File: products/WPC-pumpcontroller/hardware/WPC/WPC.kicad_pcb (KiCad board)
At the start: 2 copper layers, 97.4 x 49.1 mm, 49 parts, among them J1 NoPWR_CONN, J2 Conn_Coaxial_Small, J3 PWR_CONN, J4 Conn_IN, U13 AMS1117-5.0, U5 ESP32 30 Pin CP2102 Developme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, U7 ISC-SX1262-B, U8 AP2112K-3.3

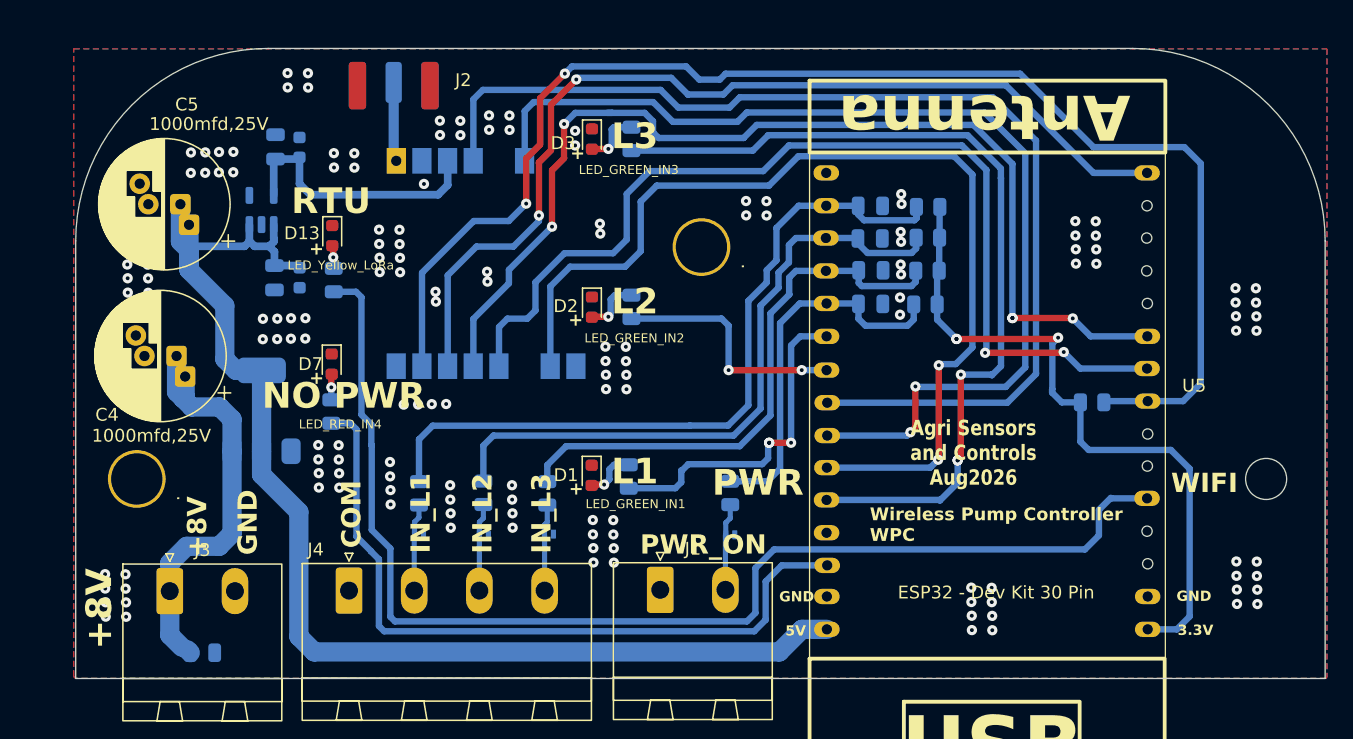
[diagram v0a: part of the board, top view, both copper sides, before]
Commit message: WPC: PumpNode + WPC board updates, add 2x panel and Gerber exports
- Update PumpNode and WPC KiCad PCB/schematic/project-local files
- Add WPC-panel2x (2-up panelized PumpNode layout) KiCad project
- Add Gerber/drill export sets for PumpNode and the 2x panel

Co-Authored-By: Claude Sonnet 5 <noreply@anthropic.com>
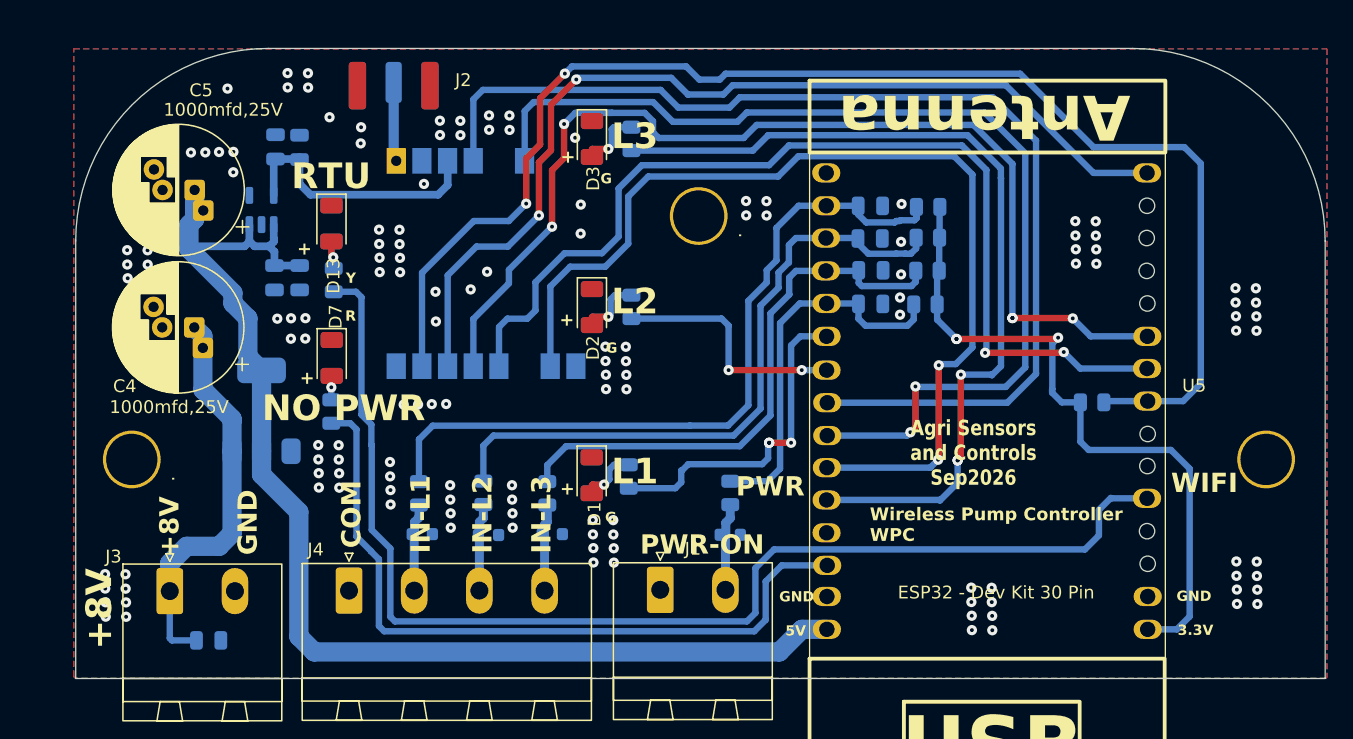
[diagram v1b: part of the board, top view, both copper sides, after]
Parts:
- C10, C12: value 10mfd,10V tentalum -> 10mfd,10V Tent; footprint Capacitor_SMD:C_0603_1608Metric -> Capacitor_SMD:C_0805_2012Metric
- D1, D13, D2, D3, D7: footprint LED_SMD:LED_0603_1608Metric -> LED_SMD:LED_1206_3216Metric
- D4, D5, D6, D8: footprint Diode_SMD:D_SOD-882 -> Diode_SMD:D_0603_1608Metric
- moved C4 2.62 mm to (169.3, 48.2)
- moved . 2.43 mm to (208.7, 39.5)
- moved C5 1.57 mm to (169.4, 37.5)
- moved . 1.57 mm to (164.5, 58.5)
- moved . 1.52 mm to (252.9, 58.5)
- moved C6 1.07 mm to (170.5, 72.6)
- moved D13 0.95 mm to (180.0, 40.1)
- moved D7 0.48 mm to (180.1, 50.6)
- moved D6 0.36 mm to (192.3, 64.4)
- moved D4 0.26 mm to (197.2, 64.3)
- moved D5 0.26 mm to (187.1, 64.3)
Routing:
- net +5V: track 98.1 -> 95.3 mm
- net +8V: track 32.5 -> 31.1 mm
- net Net-(D7-A): track 2.01 -> 2.91 mm
- net GND: vias 149 -> 138
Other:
- board text added: "Agri Sensors and Controls Sep2026"
- board text added: "D4,5,6,8 -PESD"
- board text added: "G"
- board text added: "IN-L1"
- board text added: "IN-L2"
- board text added: "IN-L3"
- board text added: "PWR-ON"
- board text added: "R"
- board text added: "Y"
- board text removed: "Agri Sensors and Controls Aug2026"
- board text removed: "IN_L1"
- board text removed: "IN_L2"
- board text removed: "IN_L3"
- board text removed: "PWR_ON"

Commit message: WPC: update PumpNode/WPC/WPC-panel2x boards, regenerate fab outputs
- Update PumpNode, WPC, and WPC-panel2x KiCad PCB/schematic/project-local
  files
- Regenerate Gerber/drill exports for all three boards
- Add a separate fab_output/ Gerber set for WPC-panel2x alongside its
  existing GERBER-FLOW/ export
- Replace the old PumpNode/WPC-panel2x fab zip archives with freshly
  regenerated ones

Co-Authored-By: Claude Sonnet 5 <noreply@anthropic.com>
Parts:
- removed H1, H2, H4, H5: MountingHole, MountingHole:MountingHole_3.2mm_M3
- moved C6 1.05 mm to (170.3, 71.5)
- moved J2 0.46 mm to (184.9, 29.6)
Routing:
- net +5V: track 95.3 -> 101.3 mm, vias 0 -> 7
- net +8V: track 31.1 -> 29.7 mm
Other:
- board size 97.4 x 49.1 mm -> 95.5 x 45.6 mm
